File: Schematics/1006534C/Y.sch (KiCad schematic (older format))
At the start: 8 parts, among them T201 2:1, X201 Transistor-NPN-body

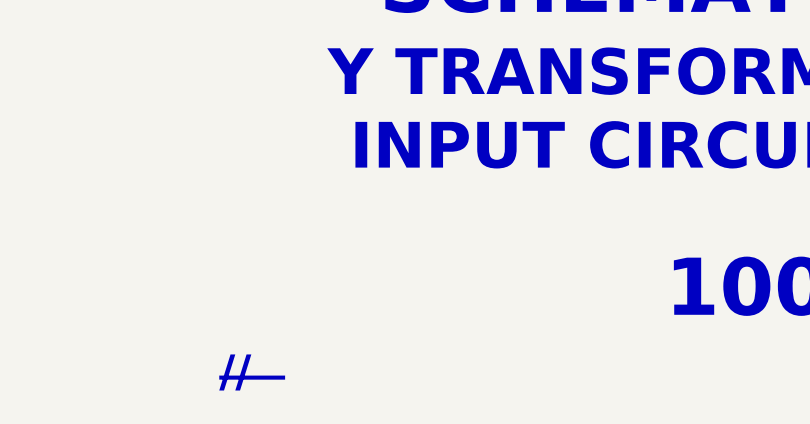
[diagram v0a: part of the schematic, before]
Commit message: Realized that the page-size indications in the title blocks were wrong.
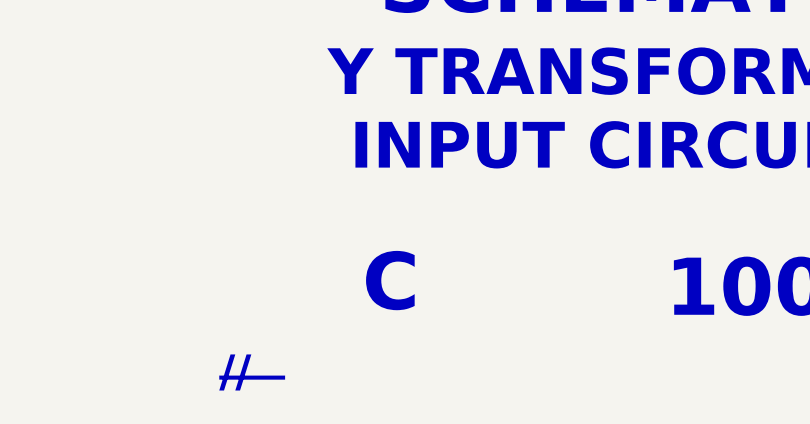
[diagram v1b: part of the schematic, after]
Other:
- note added: "C"
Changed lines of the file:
@@
 $Descr C 22000 17000
 encoding utf-8
-Sheet 2 36
+Sheet 7 36
 Title ""
 Date ""
@@
 AR Path="/5DD059AC/5C5C7C04" Ref="N3505"  Part="1"
 AR Path="/5DD1ABA8/5C5C7C04" Ref="N3603"  Part="1"
-F 0 "N3607" H 3600 6475 50  0001 C CNN
+F 0 "N2103" H 3600 6475 50  0001 C CNN
 F 1 "NodeGBody" H 3600 6550 50  0001 C CNN
 F 2 "" H 3600 6675 50  0001 C CNN
@@
 AR Path="/5DD059AC/5C5C7D6A" Ref="N3506"  Part="1"
 AR Path="/5DD1ABA8/5C5C7D6A" Ref="N3604"  Part="1"
-F 0 "N3608" H 3600 6950 50  0001 C CNN
+F 0 "N2104" H 3600 6950 50  0001 C CNN
 F 1 "NodeGBody" H 3600 7025 50  0001 C CNN
 F 2 "" H 3600 7150 50  0001 C CNN
@@
 AR Path="/5DD059AC/5C5C805E" Ref="N3504"  Part="1"
 AR Path="/5DD1ABA8/5C5C805E" Ref="N3602"  Part="1"
-F 0 "N3606" H 2500 7750 50  0001 C CNN
+F 0 "N2102" H 2500 7750 50  0001 C CNN
 F 1 "NodeGBody" H 2500 7825 50  0001 C CNN
 F 2 "" H 2500 7950 50  0001 C CNN
@@
 AR Path="/5DD059AC/5C5C82EE" Ref="N3503"  Part="1"
 AR Path="/5DD1ABA8/5C5C82EE" Ref="N3601"  Part="1"
-F 0 "N3605" H 1350 6650 50  0001 C CNN
+F 0 "N2101" H 1350 6650 50  0001 C CNN
 F 1 "NodeGBody" H 1350 6725 50  0001 C CNN
 F 2 "" H 1350 6850 50  0001 C CNN
@@
 AR Path="/5DD059AC/5C5CBE8D" Ref="R3504"  Part="1"
 AR Path="/5DD1ABA8/5C5CBE8D" Ref="R3602"  Part="1"
-F 0 "R3604" H 9825 7125 130 0001 C CNN
+F 0 "R2102" H 9825 7125 130 0001 C CNN
 F 1 "470" H 9775 6675 130 0000 C CNB
 F 2 "" H 9750 6900 130 0001 C CNN
@@
 AR Path="/5DD059AC/5C5CCF55" Ref="R3503"  Part="1"
 AR Path="/5DD1ABA8/5C5CCF55" Ref="R3601"  Part="1"
-F 0 "R3603" V 9050 7700 130 0001 C CNN
+F 0 "R2101" V 9050 7700 130 0001 C CNN
 F 1 "51" V 9275 7675 130 0000 C CNB
 F 2 "" H 9300 7300 130 0001 C CNN
@@
 AR Path="/5DD059AC/5C5E4D5C" Ref="T3501"  Part="1"
 AR Path="/5DD1ABA8/5C5E4D5C" Ref="T3601"  Part="1"
-F 0 "T3602" H 7300 8250 130 0001 C CNN
+F 0 "T2101" H 7300 8250 130 0001 C CNN
 F 1 "2:1" H 7300 7950 130 0000 C CNB
 F 2 "" V 7250 6650 130 0001 C CNN
@@
 AR Path="/5DD059AC/5C5E5AC8" Ref="X3503"  Part="1"
 AR Path="/5DD1ABA8/5C5E5AC8" Ref="X3601"  Part="1"
-F 0 "X3602" H 11325 7315 130 0001 C CNN
+F 0 "X2101" H 11325 7315 130 0001 C CNN
 F 1 "Transistor-NPN-body" H 11325 7465 130 0001 C CNN
 F 2 "" H 11325 7150 130 0001 C CNN
@@
 Wire Notes Line width 60 style solid
 	3300 7200 3175 7150
+Text Notes 17600 16100 0    250  ~ 50
+C
 $EndSCHEMATC

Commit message: Drawing set 1006534C+1006088A+1006087B has been reannotated.  Given that there are no INSULATOR drawings available (or even known) for them, this annotation is undoubtedly incorrect in some details.
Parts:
- removed X201: Transistor-NPN-body, symbol AGC_DSKY:Transistor-NPN-body
- added X1701: Transistor-NPN-body, symbol AGC_DSKY:Transistor-NPN-body
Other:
- note added: "Q1"
